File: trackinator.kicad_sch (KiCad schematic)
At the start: 33 parts, among them J1 Conn_01x04_Pin, SW1 TS-1187A-B-A-B, SW2 TS-1187A-B-A-B, U1 M24C02-WMN, U5 SP3481EN, U6 FE2.1, U7 SP3481EN, U8 SP3481EN, Y1 12Mhz

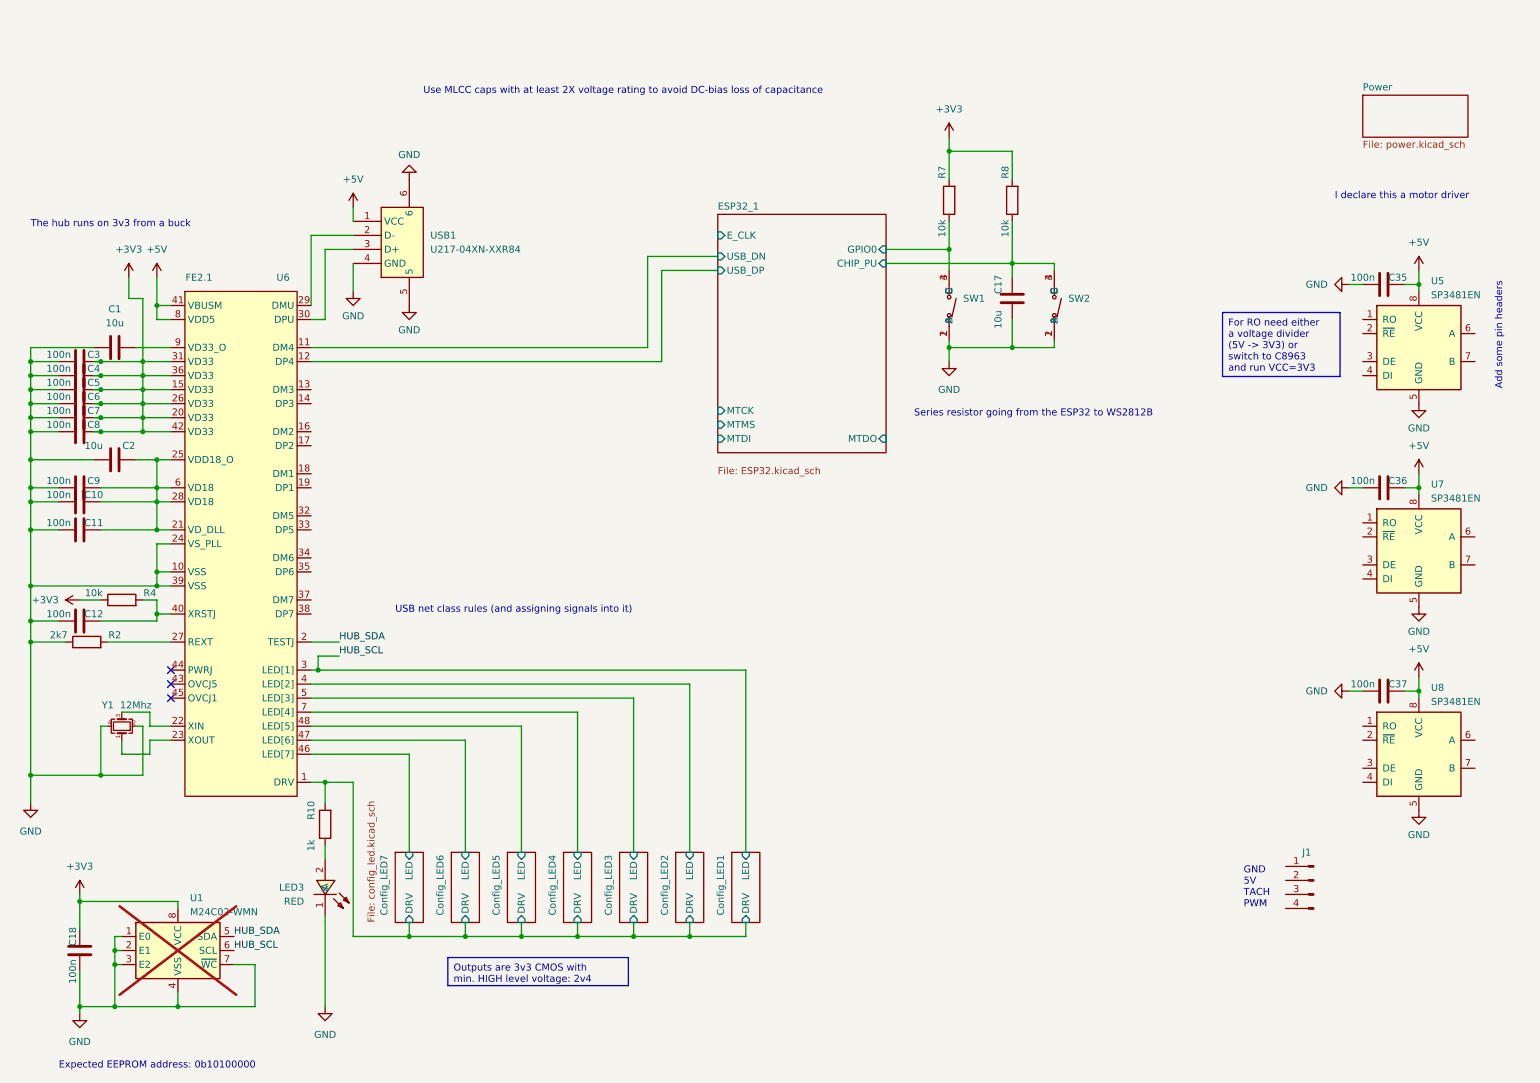
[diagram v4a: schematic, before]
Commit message: more connectors and USB
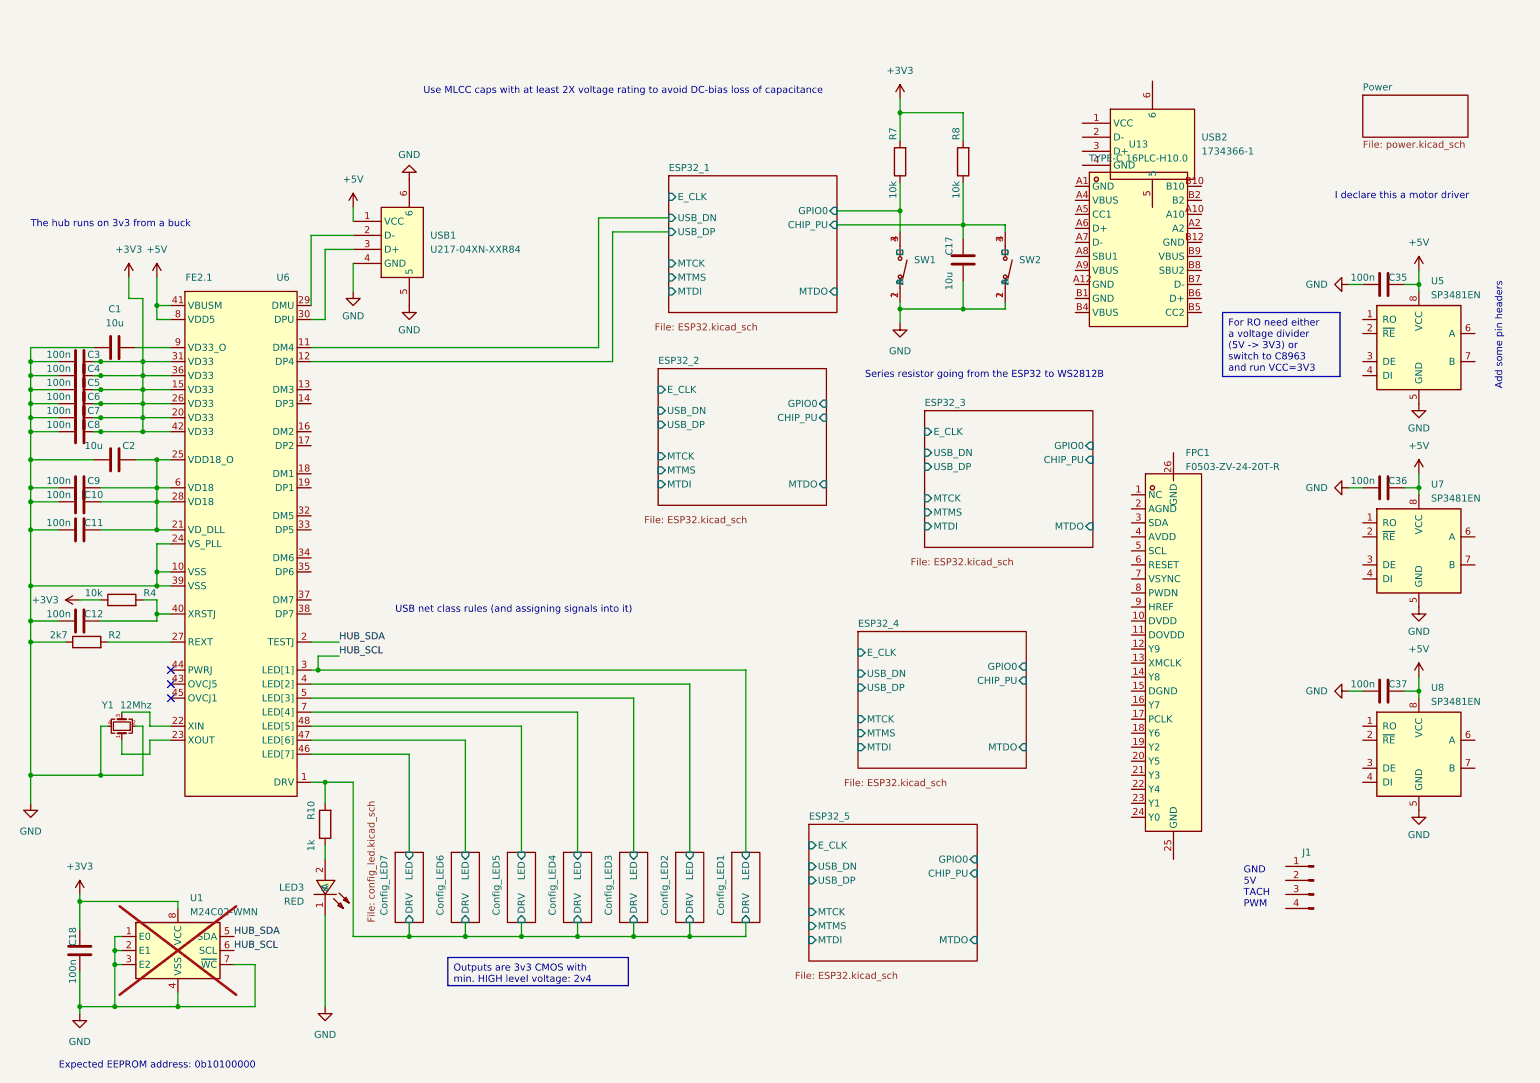
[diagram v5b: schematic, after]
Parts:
- added FPC1: F0503-ZV-24-20T-R, easyeda2kicad:FPC-SMD_F0503-ZV-24-20T-R, symbol easyeda2kicad:F0503-ZV-24-20T-R
- added U13: TYPE-C 16PLC-H10.0, easyeda2kicad:TYPE-C-TH_16PLC-H10.0, symbol easyeda2kicad:TYPE-C16PLC-H10.0
- added USB2: 1734366-1, easyeda2kicad:USB-A-TH_FUS264-FDSW3K, symbol easyeda2kicad:1734366-1
- J1: footprint (none) -> Connector:FanPinHeader_1x04_P2.54mm_Vertical
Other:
- added sheet ESP32_2 (ESP32.kicad_sch)
- added sheet ESP32_3 (ESP32.kicad_sch)
- added sheet ESP32_4 (ESP32.kicad_sch)
- added sheet ESP32_5 (ESP32.kicad_sch)
- moved on the sheet: C17, R7, R8, SW1, SW2

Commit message: savin' my work!
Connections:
- net at U13.A1 (GND): now also U13.A12 (GND), U13.B1 (GND), U13.B12 (GND)
- net at U13.A10 (SHIELD): now also U13.A2 (SHIELD), U13.B10 (SHIELD), U13.B2 (SHIELD)
- net at U13.A4 (VBUS): now also U13.A9 (VBUS), U13.B4 (VBUS), U13.B9 (VBUS)
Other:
- moved on the sheet: USB2
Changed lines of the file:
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@@
     )
   )
-  (symbol (lib_id "easyeda2kicad:TYPE-C16PLC-H10.0") (at 215.9 45.72 0) (unit 1)
-    (in_bom yes) (on_board yes) (dnp no) (fields_autoplaced)
-    (property "Reference" "U13" (at 215.9 26.67 0)
-      (effects (font (size 1.27 1.27)))
-    )
-    (property "Value" "TYPE-C 16PLC-H10.0" (at 215.9 29.21 0)
-      (effects (font (size 1.27 1.27)))
-    )
-    (property "Footprint" "easyeda2kicad:TYPE-C-TH_16PLC-H10.0" (at 215.9 64.77 0)
-      (effects (font (size 1.27 1.27)) hide)
-    )
-    (property "Datasheet" "" (at 215.9 45.72 0)
-      (effects (font (size 1.27 1.27)) hide)
-    )
-    (property "LCSC Part" "C3151747" (at 215.9 67.31 0)
+  (symbol (lib_id "easyeda2kicad:TYPE-C16PLC-H10.0") (at 215.9 46.99 0) (unit 1)
+    (in_bom yes) (on_board yes) (dnp no) (fields_autoplaced)
+    (property "Reference" "U13" (at 215.9 27.94 0)
+      (effects (font (size 1.27 1.27)))
+    )
+    (property "Value" "TYPE-C 16PLC-H10.0" (at 215.9 30.48 0)
+      (effects (font (size 1.27 1.27)))
+    )
+    (property "Footprint" "easyeda2kicad:TYPE-C-TH_16PLC-H10.0" (at 215.9 66.04 0)
+      (effects (font (size 1.27 1.27)) hide)
+    )
+    (property "Datasheet" "" (at 215.9 46.99 0)
+      (effects (font (size 1.27 1.27)) hide)
+    )
+    (property "LCSC Part" "C3151747" (at 215.9 68.58 0)
       (effects (font (size 1.27 1.27)) hide)
     )
@@
     )
   )
-  (symbol (lib_id "easyeda2kicad:1734366-1") (at 215.9 27.94 0) (unit 1)
-    (in_bom yes) (on_board yes) (dnp no) (fields_autoplaced)
-    (property "Reference" "USB2" (at 227.33 25.4 0)
+  (symbol (lib_id "easyeda2kicad:1734366-1") (at 214.63 15.24 0) (unit 1)
+    (in_bom yes) (on_board yes) (dnp no) (fields_autoplaced)
+    (property "Reference" "USB2" (at 226.06 12.7 0)
       (effects (font (size 1.27 1.27)) (justify left))
     )
-    (property "Value" "1734366-1" (at 227.33 27.94 0)
+    (property "Value" "1734366-1" (at 226.06 15.24 0)
       (effects (font (size 1.27 1.27)) (justify left))
     )
-    (property "Footprint" "easyeda2kicad:USB-A-TH_FUS264-FDSW3K" (at 215.9 45.72 0)
-      (effects (font (size 1.27 1.27)) hide)
-    )
-    (property "Datasheet" "" (at 215.9 27.94 0)
-      (effects (font (size 1.27 1.27)) hide)
-    )
-    (property "LCSC Part" "C305910" (at 215.9 48.26 0)
-      (effects (font (size 1.27 1.27)) hide)
-    )
+    (property "Footprint" "easyeda2kicad:USB-A-TH_FUS264-FDSW3K" (at 214.63 33.02 0)
+      (effects (font (size 1.27 1.27)) hide)
+    )
+    (property "Datasheet" "" (at 214.63 15.24 0)
+      (effects (font (size 1.27 1.27)) hide)
+    )
+    (property "LCSC Part" "C305910" (at 214.63 35.56 0)
+      (effects (font (size 1.27 1.27)) hide)
+    )
